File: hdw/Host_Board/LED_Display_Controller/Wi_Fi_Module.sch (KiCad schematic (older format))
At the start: 0 parts

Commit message: Added WIFI module, some more editing
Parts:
- added C?: 0.1uF, symbol LED_Display_Local_Library:C_Custom
- added J?: ESP8266_Socket, symbol Connector_Generic:Conn_02x04_Odd_Even
- added Q?: 2N7002, Housings_SOIC:PowerPAK_SO-8_Single, symbol Custom_Library:2N7002
- added R? (x5): 10k, symbol LED_Display_Local_Library:R_Custom
- added R?: 100, symbol LED_Display_Local_Library:R_Custom
- added R?: 10, symbol LED_Display_Local_Library:R_Custom
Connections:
- new net: C?.1, J?.6 (Pin_6), R?.2, R?.2
- new net: Q?.4 (G), R?.2, R?.2
- new net: Q?.5 (D), R?.1
- new net +3V3: J?.8 (Pin_8), R?.1, R?.1, R?.1, R?.1
- new net GND: C?.2, J?.1 (Pin_1), Q?.1 (S), Q?.2 (S), Q?.3 (S), R?.2
- new net WIFI_CHPD: J?.4 (Pin_4), R?.1
- new net WIFI_UART_RX: J?.7 (Pin_7), R?.2
- new net WIFI_UART_TX: J?.2 (Pin_2), R?.2
- new net ~WIFI_RESET: R?.1
- no-connect marks 0 -> 2
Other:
- note added: "ESP8266 Pinout does not match default KiCad pin socket footprint. \nAlter the pin numbers in layout"

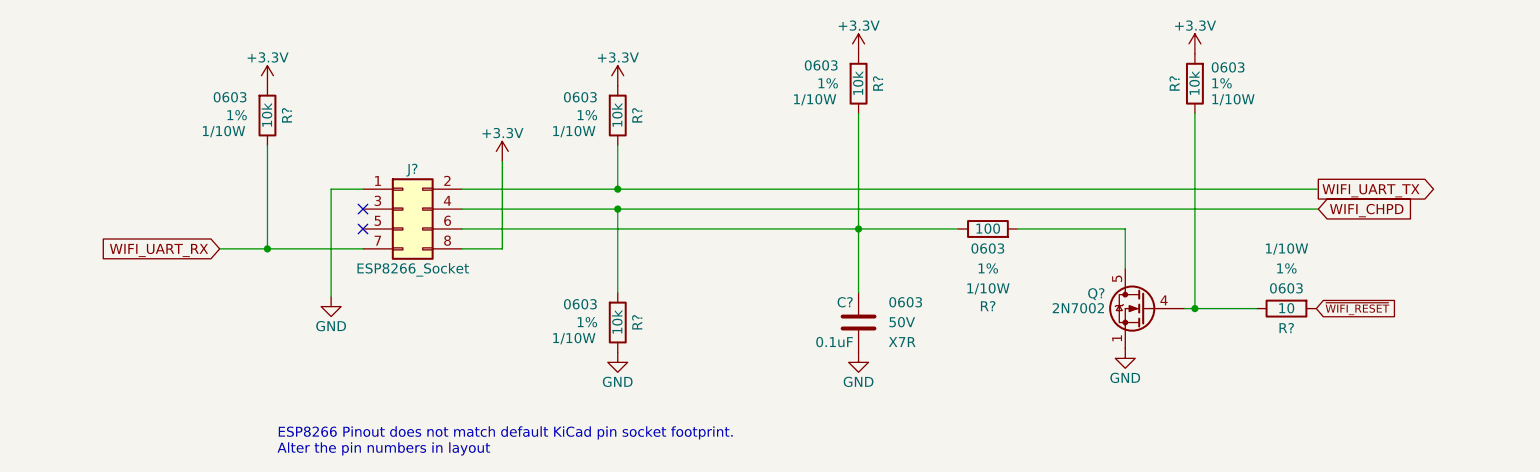
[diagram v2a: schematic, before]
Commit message: Added a few pages for more features
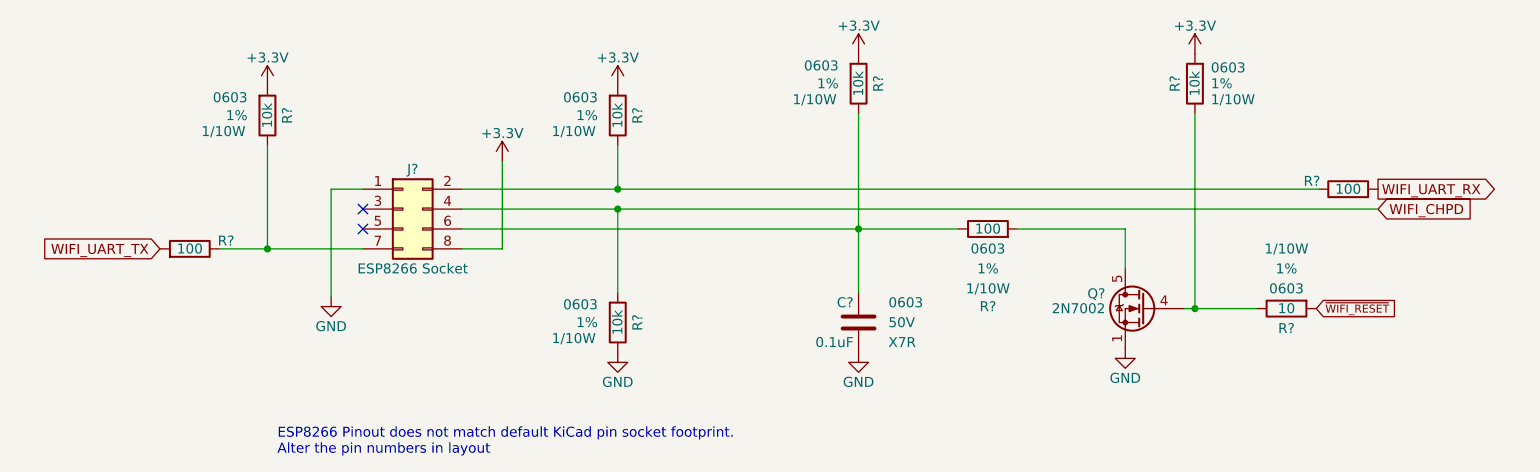
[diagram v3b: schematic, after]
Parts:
- added R? (x2): 100, symbol LED_Display_Local_Library:R_Custom
- J?: value ESP8266_Socket -> ESP8266 Socket
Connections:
- net WIFI_UART_RX: now also R?.1; no longer J?.7 (Pin_7), R?.2
- net WIFI_UART_TX: now also R?.1; no longer J?.2 (Pin_2), R?.2
- new net: J?.2 (Pin_2), R?.2, R?.2
- new net: J?.7 (Pin_7), R?.2, R?.2
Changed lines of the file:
@@
 $Descr A 11000 8500
 encoding utf-8
-Sheet 5 25
+Sheet 5 30
 Title ""
 Date ""
@@
 P 3700 3540
 F 0 "J?" H 3750 3740 50  0000 C CNN
-F 1 "ESP8266_Socket" H 3750 3240 50  0000 C CNN
+F 1 "ESP8266 Socket" H 3750 3240 50  0000 C CNN
 F 2 "" H 3700 3540 50  0001 C CNN
 F 3 "~" H 3700 3540 50  0001 C CNN
@@
 Wire Wire Line
 	3340 3440 3500 3440
-Text GLabel 8300 3440 2    50   Output ~ 0
-WIFI_UART_TX
-Text GLabel 8300 3540 2    50   Input ~ 0
+Text GLabel 8600 3440 2    50   Output ~ 0
+WIFI_UART_RX
+Text GLabel 8600 3540 2    50   Input ~ 0
 WIFI_CHPD
 Text GLabel 8290 4040 2    40   Input ~ 0
@@
 Wire Wire Line
 	4200 3740 4000 3740
-Text GLabel 2780 3740 0    50   Input ~ 0
-WIFI_UART_RX
+Text GLabel 2480 3740 0    50   Input ~ 0
+WIFI_UART_TX
 $Comp
 L LED_Display_Local_Library:C_Custom C?
@@
 	4780 3440 8300 3440
 Connection ~ 4780 3440
-Wire Wire Line
-	4780 3540 8300 3540
 Connection ~ 4780 3540
 Wire Wire Line
 	4000 3640 5990 3640
+$Comp
+L LED_Display_Local_Library:R_Custom R?
+U 1 1 5BE3C385
+P 8450 3440
+AR Path="/5BAAE2B6/5BE3C385" Ref="R?"  Part="1"
+AR Path="/5BB6CF6D/5BE3C385" Ref="R?"  Part="1"
+AR Path="/5BBE424C/5BE3C385" Ref="R?"  Part="1"
+AR Path="/5BAAE1CB/5BE3C385" Ref="R?"  Part="1"
+F 0 "R?" V 8410 3300 50  0000 R CNN
+F 1 "100" V 8450 3440 50  0000 C CNN
+F 2 "" H 8450 3440 50  0001 C CNN
+F 3 "" H 8450 3440 50  0001 C CNN
+F 4 "0603" V 8550 3440 50  0001 C CNN "display_footprint"
+F 5 "1%" V 8650 3440 50  0001 C CNN "Tolerance"
+F 6 "1/10W" V 8750 3440 50  0001 C CNN "Wattage"
+F 7 "PN" H 8750 3840 60  0001 C CNN "Digi-Key PN"
+	1    8450 3440
+	0    1    1    0
+$EndComp
+$Comp
+L LED_Display_Local_Library:R_Custom R?
+U 1 1 5BE3C39B
+P 2630 3740
+AR Path="/5BAAE2B6/5BE3C39B" Ref="R?"  Part="1"
+AR Path="/5BB6CF6D/5BE3C39B" Ref="R?"  Part="1"
+AR Path="/5BBE424C/5BE3C39B" Ref="R?"  Part="1"
+AR Path="/5BAAE1CB/5BE3C39B" Ref="R?"  Part="1"
+F 0 "R?" V 2590 3600 50  0000 R CNN
+F 1 "100" V 2630 3740 50  0000 C CNN
+F 2 "" H 2630 3740 50  0001 C CNN
+F 3 "" H 2630 3740 50  0001 C CNN
+F 4 "0603" V 2730 3740 50  0001 C CNN "display_footprint"
+F 5 "1%" V 2830 3740 50  0001 C CNN "Tolerance"
+F 6 "1/10W" V 2930 3740 50  0001 C CNN "Wattage"
+F 7 "PN" H 2930 4140 60  0001 C CNN "Digi-Key PN"
+	1    2630 3740
+	0    -1   1    0
+$EndComp
+Wire Wire Line
+	4780 3540 8600 3540
 $EndSCHEMATC

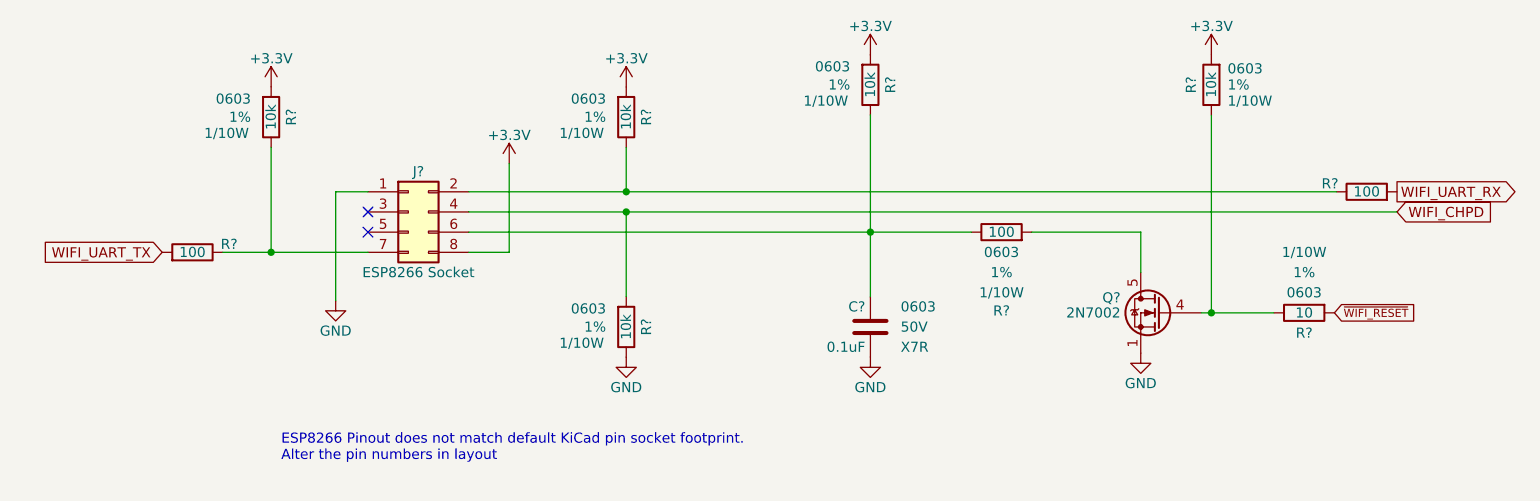
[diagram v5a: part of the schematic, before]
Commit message: Added graphical symbols to certain sheets
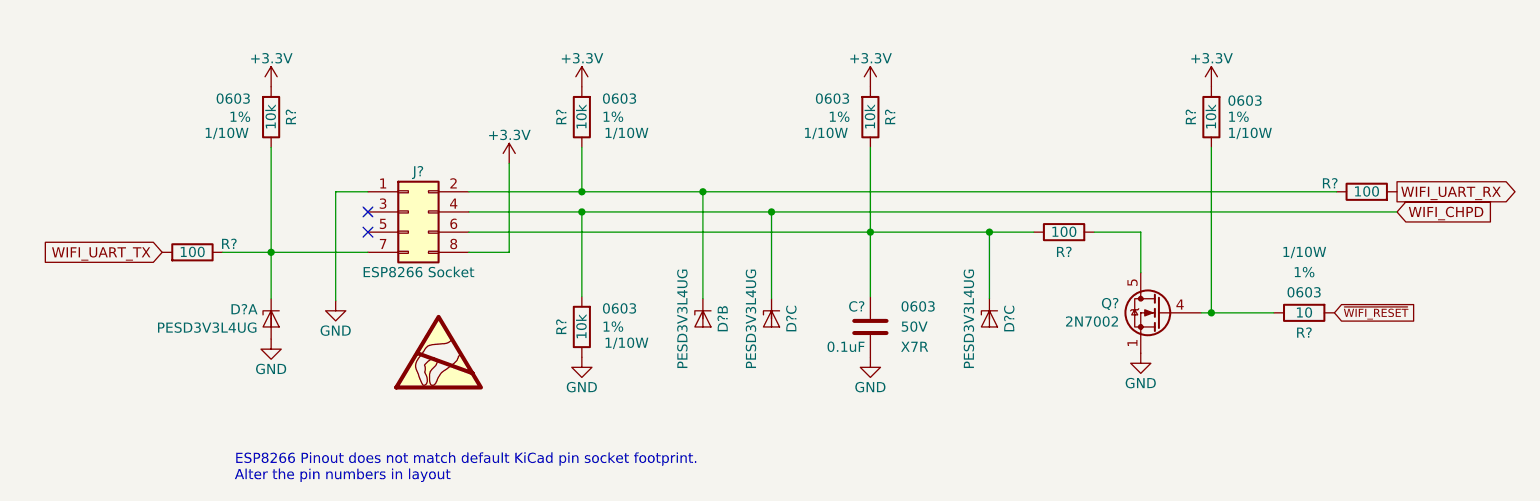
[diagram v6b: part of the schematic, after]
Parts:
- added D? (x4): PESD3V3L4UG, Package_TO_SOT_SMD:SOT-353_SC-70-5, symbol Power_Protection:PESD3V3L4UG
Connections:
- net GND: now also D?.2 (A)
- net WIFI_CHPD: now also D?.4 (K3)
- net at J?.2 (Pin_2), R?.2, R?.2: now also D?.3 (K2)
- net at C?.1, J?.6 (Pin_6), R?.2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: now also D?.4 (K3)
- net at J?.7 (Pin_7), R?.2, R?.2: now also D?.1 (K1)
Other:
- moved on the sheet: R?

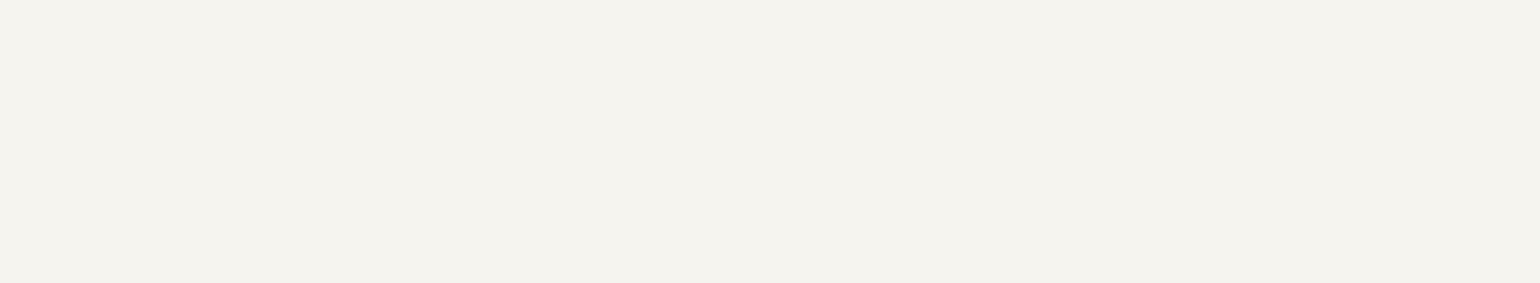
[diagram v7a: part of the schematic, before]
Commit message: Added titles and MU logo to each sheet
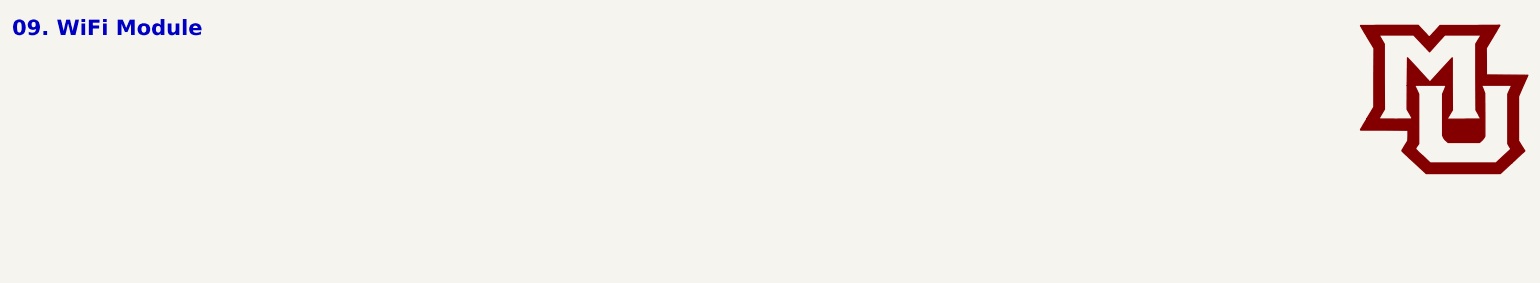
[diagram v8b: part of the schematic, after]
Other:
- note added: "09. WiFi Module"
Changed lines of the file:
@@
+	1    0    0    -1
+$EndComp
+Text Notes 550  700  0    100  ~ 20
+09. WiFi Module
+$Comp
+L LED_Display_Local_Library:MU_Logo #G?
+U 1 1 5BFF302C
+P 9900 1100
+F 0 "#G?" H 9900 614 60  0001 C CNN
+F 1 "MU_Logo" H 9900 1586 60  0001 C CNN
+F 2 "" H 9900 1100 50  0001 C CNN
+F 3 "" H 9900 1100 50  0001 C CNN
+	1    9900 1100
 	1    0    0    -1
 $EndComp
